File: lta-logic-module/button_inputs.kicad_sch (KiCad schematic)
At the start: 26 parts, among them J5 Conn_01x12, U11 SN74LVC14AD, U12 SN74LVC14AD

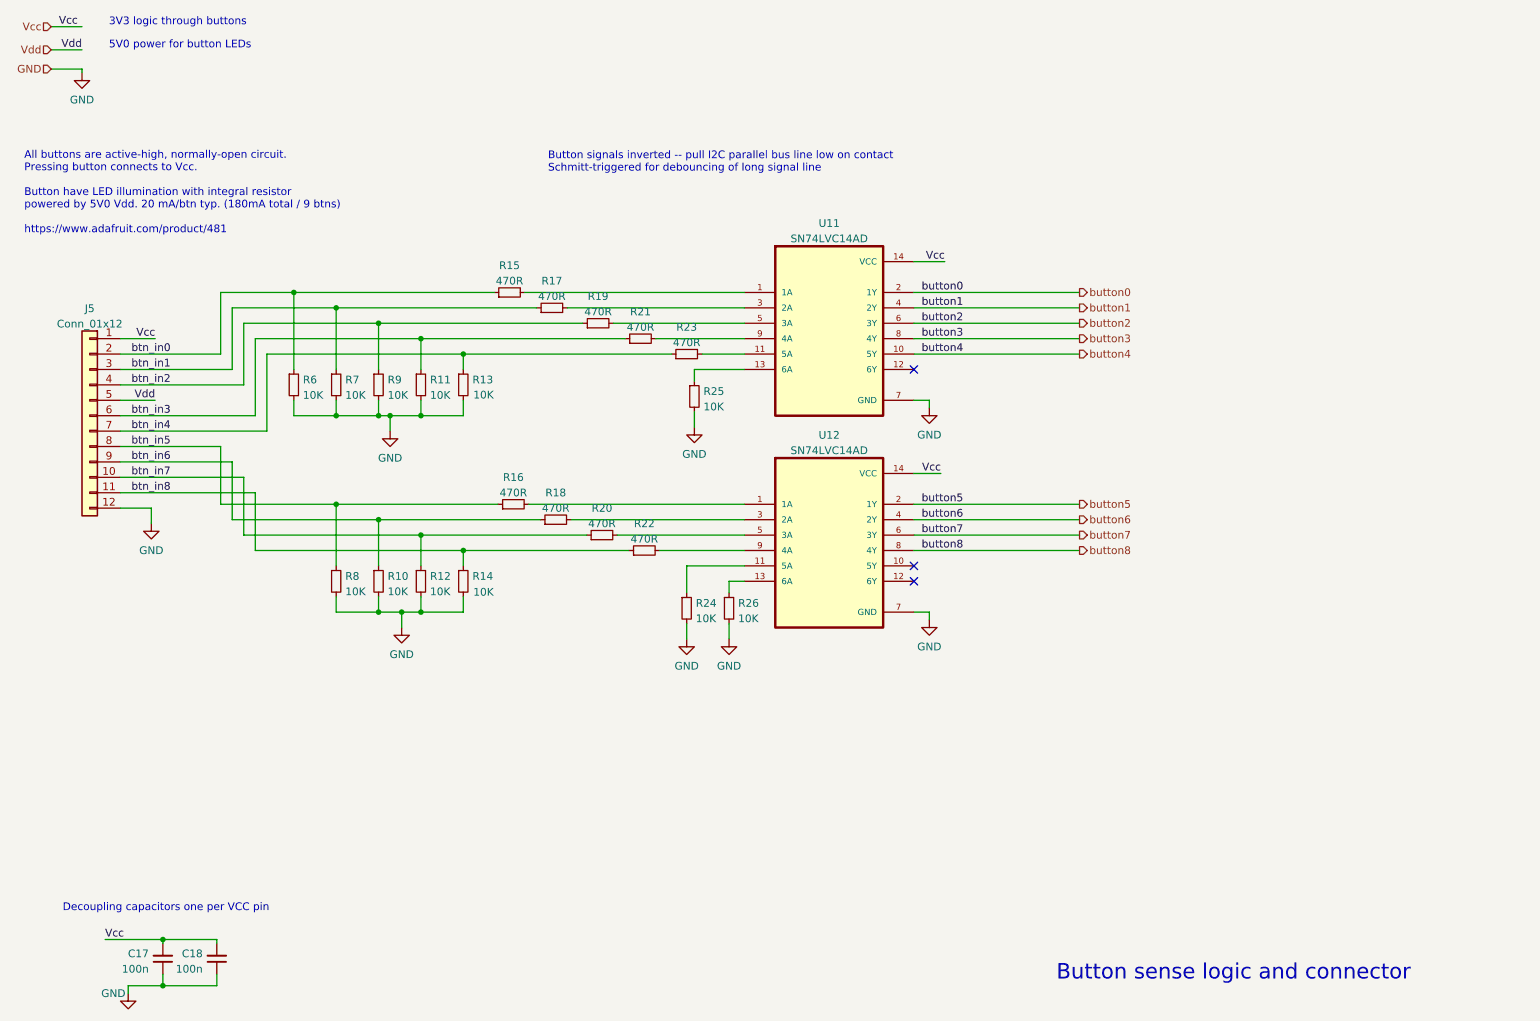
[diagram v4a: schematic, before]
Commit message: Add light sensor circuit.
Adjust TODOs and comments after testing btn circuit.
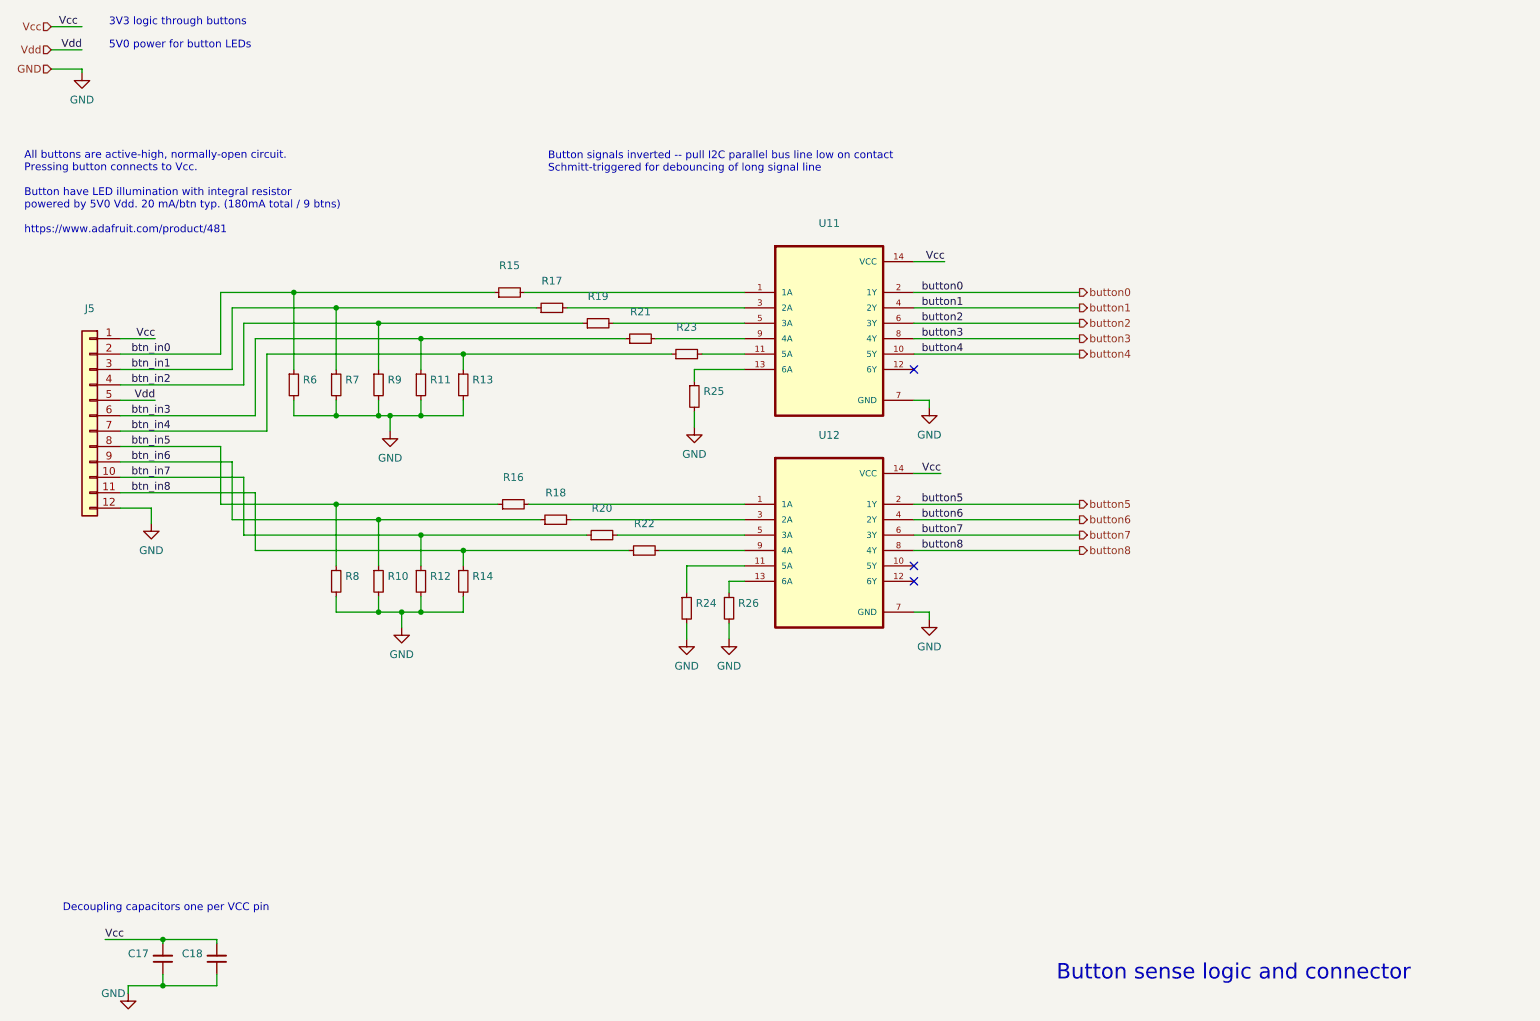
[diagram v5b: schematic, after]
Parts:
- C17, C18: value 100n -> (none); footprint Capacitor_SMD:C_0603_1608Metric -> (none)
- J5: value Conn_01x12 -> (none); footprint Connector_PinHeader_2.54mm:PinHeader_1x12_P2.54mm_Vertical -> (none)
- R10, R11, R12, R13, R14, R24, R25, R26, R6, R7, R8, R9: value 10K -> (none); footprint Resistor_SMD:R_0603_1608Metric -> (none)
- R15, R16, R17, R18, R19, R20, R21, R22, R23: value 470R -> (none); footprint Resistor_SMD:R_0603_1608Metric -> (none)
- U11, U12: value SN74LVC14AD -> (none); footprint Aaron_TI_Parts:TI_SOIC_D_R-PDSO-G14 -> (none)

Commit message: Add main draft of PCB layout for logic module.
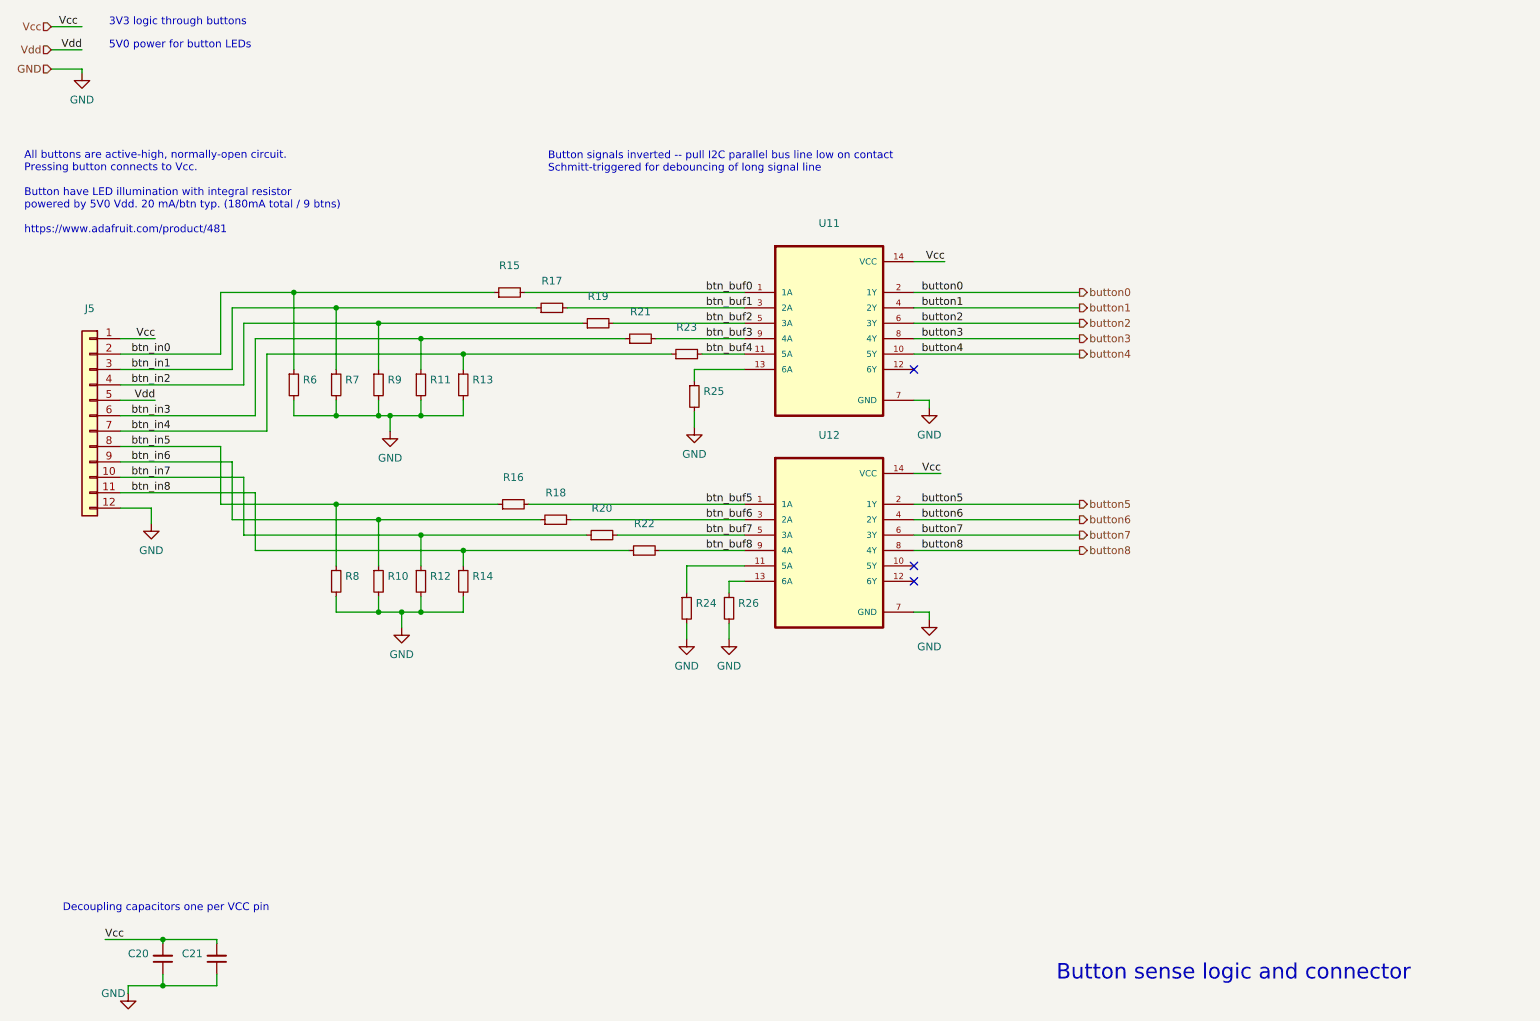
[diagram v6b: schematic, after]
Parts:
- U11, U12: Comment (none) -> Exact MFR/MPN required
- renumbered C17 to C20, C18 to C21
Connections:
- net btn_buf6: now reaches R18.2, U12.3 (2A)
- net btn_buf8: now reaches R22.2, U12.9 (4A)
- net btn_buf2: now reaches R19.2, U11.5 (3A)
- net btn_buf7: now reaches R20.2, U12.5 (3A)
- net btn_buf5: now reaches R16.2, U12.1 (1A)
- net btn_buf3: now reaches R21.2, U11.9 (4A)
- net btn_buf0: now reaches R15.2, U11.1 (1A)
- net btn_buf4: now reaches R23.2, U11.11 (5A)
- net btn_buf1: now reaches R17.2, U11.3 (2A)
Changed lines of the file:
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@@
     (effects (font (size 1.27 1.27)) (justify right bottom))
+  )
+  (label "btn_buf2" (at 128.27 66.675 0)
+    (effects (font (size 1.27 1.27)) (justify left bottom))
   )
   (label "Vcc" (at 37.465 69.215 180)
@@
     (effects (font (size 1.27 1.27)) (justify left bottom))
   )
+  (label "btn_buf4" (at 128.27 71.755 0)
+    (effects (font (size 1.27 1.27)) (justify left bottom))
+  )
   (label "Vdd" (at 37.465 79.375 180)
     (effects (font (size 1.27 1.27)) (justify right bottom))
   )
+  (label "btn_buf1" (at 128.27 64.135 0)
+    (effects (font (size 1.27 1.27)) (justify left bottom))
+  )
   (label "btn_in2" (at 40.005 76.835 180)
     (effects (font (size 1.27 1.27)) (justify right bottom))
@@
     (effects (font (size 1.27 1.27)) (justify right bottom))
   )
+  (label "btn_buf8" (at 128.27 104.14 0)
+    (effects (font (size 1.27 1.27)) (justify left bottom))
+  )
   (label "Vcc" (at 21.59 17.78 0)
     (effects (font (size 1.27 1.27)) (justify left bottom))
   )
+  (label "btn_buf0" (at 128.27 61.595 0)
+    (effects (font (size 1.27 1.27)) (justify left bottom))
+  )
   (label "btn_in3" (at 40.005 81.915 180)
     (effects (font (size 1.27 1.27)) (justify right bottom))
   )
+  (label "btn_buf5" (at 128.27 96.52 0)
+    (effects (font (size 1.27 1.27)) (justify left bottom))
+  )
   (label "button0" (at 163.83 61.595 0)
     (effects (font (size 1.27 1.27)) (justify left bottom))
@@
     (effects (font (size 1.27 1.27)) (justify right bottom))
   )
+  (label "btn_buf6" (at 128.27 99.06 0)
+    (effects (font (size 1.27 1.27)) (justify left bottom))
+  )
+  (label "btn_buf3" (at 128.27 69.215 0)
+    (effects (font (size 1.27 1.27)) (justify left bottom))
+  )
   (label "btn_in6" (at 40.005 89.535 180)
     (effects (font (size 1.27 1.27)) (justify right bottom))
@@
   (label "btn_in8" (at 40.005 94.615 180)
     (effects (font (size 1.27 1.27)) (justify right bottom))
+  )
+  (label "btn_buf7" (at 128.27 101.6 0)
+    (effects (font (size 1.27 1.27)) (justify left bottom))
   )
   (label "button8" (at 163.83 104.14 0)
@@
   (symbol (lib_id "power:GND") (at 36.83 99.695 0) (unit 1)
     (in_bom yes) (on_board yes) (fields_autoplaced)
-    (property "Reference" "#PWR046" (id 0) (at 36.83 106.045 0)
+    (property "Reference" "#PWR047" (id 0) (at 36.83 106.045 0)
       (effects (font (size 1.27 1.27)) hide)
     )
@@
   (symbol (lib_id "Device:C_Small") (at 47.625 171.45 0) (mirror x) (unit 1)
     (in_bom yes) (on_board yes) (fields_autoplaced)
-    (property "Reference" "C18" (id 0) (at 45.3009 170.6089 0)
+    (property "Reference" "C21" (id 0) (at 45.3009 170.6089 0)
       (effects (font (size 1.27 1.27)) (justify right))
     )
@@
   (symbol (lib_id "power:GND") (at 125.095 118.745 0) (unit 1)
     (in_bom yes) (on_board yes) (fields_autoplaced)
-    (property "Reference" "#PWR049" (id 0) (at 125.095 125.095 0)
+    (property "Reference" "#PWR050" (id 0) (at 125.095 125.095 0)
       (effects (font (size 1.27 1.27)) hide)
     )
@@
     )
     (property "MPN" "SN74LVC14AD" (id 5) (at 152.4 104.14 0)
+      (effects (font (size 1.27 1.27)) hide)
+    )
+    (property "Comment" "Exact MFR/MPN required" (id 6) (at 152.4 104.14 0)
       (effects (font (size 1.27 1.27)) hide)
     )
@@
   (symbol (lib_id "power:GND") (at 76.2 84.455 0) (unit 1)
     (in_bom yes) (on_board yes) (fields_autoplaced)
-    (property "Reference" "#PWR047" (id 0) (at 76.2 90.805 0)
+    (property "Reference" "#PWR048" (id 0) (at 76.2 90.805 0)
       (effects (font (size 1.27 1.27)) hide)
     )
@@
   (symbol (lib_id "power:GND") (at 126.365 83.82 0) (unit 1)
     (in_bom yes) (on_board yes) (fields_autoplaced)
-    (property "Reference" "#PWR050" (id 0) (at 126.365 90.17 0)
+    (property "Reference" "#PWR051" (id 0) (at 126.365 90.17 0)
       (effects (font (size 1.27 1.27)) hide)
     )
@@
   (symbol (lib_id "Device:C_Small") (at 38.735 171.45 0) (mirror x) (unit 1)
     (in_bom yes) (on_board yes) (fields_autoplaced)
-    (property "Reference" "C17" (id 0) (at 36.4109 170.6089 0)
+    (property "Reference" "C20" (id 0) (at 36.4109 170.6089 0)
       (effects (font (size 1.27 1.27)) (justify right))
     )
@@
   (symbol (lib_id "power:GND") (at 132.08 118.745 0) (unit 1)
     (in_bom yes) (on_board yes) (fields_autoplaced)
-    (property "Reference" "#PWR051" (id 0) (at 132.08 125.095 0)
+    (property "Reference" "#PWR052" (id 0) (at 132.08 125.095 0)
       (effects (font (size 1.27 1.27)) hide)
     )
@@
   (symbol (lib_id "power:GND") (at 165.1 115.57 0) (unit 1)
     (in_bom yes) (on_board yes) (fields_autoplaced)
-    (property "Reference" "#PWR053" (id 0) (at 165.1 121.92 0)
+    (property "Reference" "#PWR054" (id 0) (at 165.1 121.92 0)
       (effects (font (size 1.27 1.27)) hide)
     )
@@
   (symbol (lib_id "power:GND") (at 78.105 116.84 0) (unit 1)
     (in_bom yes) (on_board yes) (fields_autoplaced)
-    (property "Reference" "#PWR048" (id 0) (at 78.105 123.19 0)
+    (property "Reference" "#PWR049" (id 0) (at 78.105 123.19 0)
       (effects (font (size 1.27 1.27)) hide)
     )
@@
     )
     (property "MPN" "SN74LVC14AD" (id 5) (at 152.4 69.215 0)
+      (effects (font (size 1.27 1.27)) hide)
+    )
+    (property "Comment" "Exact MFR/MPN required" (id 6) (at 152.4 69.215 0)
       (effects (font (size 1.27 1.27)) hide)
     )
@@
   (symbol (lib_id "power:GND") (at 25.4 25.4 0) (unit 1)
     (in_bom yes) (on_board yes) (fields_autoplaced)
-    (property "Reference" "#PWR044" (id 0) (at 25.4 31.75 0)
+    (property "Reference" "#PWR045" (id 0) (at 25.4 31.75 0)
       (effects (font (size 1.27 1.27)) hide)
     )
@@
   (symbol (lib_id "power:GND") (at 33.02 177.165 0) (unit 1)
     (in_bom yes) (on_board yes)
-    (property "Reference" "#PWR045" (id 0) (at 33.02 183.515 0)
+    (property "Reference" "#PWR046" (id 0) (at 33.02 183.515 0)
       (effects (font (size 1.27 1.27)) hide)
     )
@@
   (symbol (lib_id "power:GND") (at 165.1 80.645 0) (unit 1)
     (in_bom yes) (on_board yes) (fields_autoplaced)
-    (property "Reference" "#PWR052" (id 0) (at 165.1 86.995 0)
-      (effects (font (size 1.27 1.27)) hide)
-    )
+    (property "Reference" "#PWR053" (id 0) (at 165.1 86.995 0)
+      (effects (font (size 1.27 1.27)) hide)
+    )

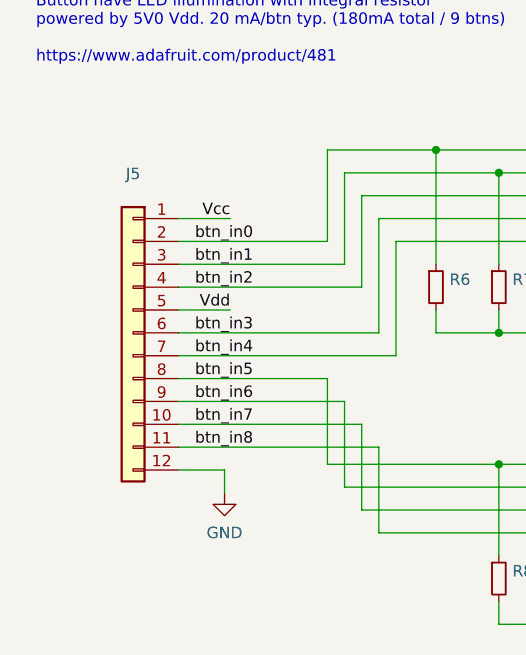
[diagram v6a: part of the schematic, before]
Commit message: Switch 12-pin headers to Molex Micro-Latch c'tors.
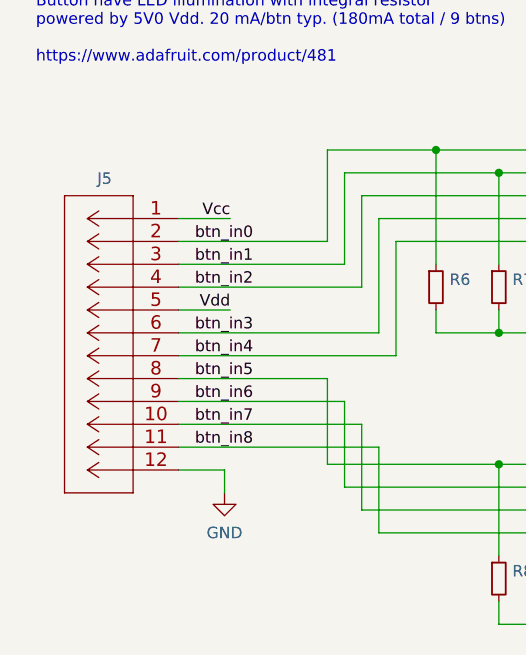
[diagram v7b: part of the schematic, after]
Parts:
- J5: symbol Connector_Generic:Conn_01x12 -> Aaron-Connectors:Molex-MicroLatch-53253-1270; Comment TODO REPLACE FOOTPRINT -> (none); MANUFACTURER (none) -> Molex; MPN XXX TODO FIND -> 532531270
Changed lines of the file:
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@@
     (pin "1")
   )
-  (symbol (lib_id "Connector_Generic:Conn_01x12") (at 26.67 81.915 0) (mirror y) (unit 1)
-    (in_bom yes) (on_board yes) (fields_autoplaced)
-    (property "Reference" "J5" (id 0) (at 26.67 64.2452 0))
-    (property "Value" "" (id 1) (at 26.67 66.7821 0))
-    (property "Footprint" "" (id 2) (at 26.67 81.915 0)
+  (symbol (lib_id "Aaron-Connectors:Molex-MicroLatch-53253-1270") (at 31.75 69.215 0) (mirror y) (unit 1)
+    (in_bom yes) (on_board yes)
+    (property "Reference" "J5" (id 0) (at 23.495 64.77 0))
+    (property "Value" "" (id 1) (at 15.875 83.82 90)
+      (effects (font (size 1.524 1.524)))
+    )
+    (property "Footprint" "" (id 2) (at 22.86 103.505 0)
+      (effects (font (size 1.524 1.524)) hide)
+    )
+    (property "Datasheet" "https://www.molex.com/webdocs/datasheets/pdf/en-us/0532531270_PCB_HEADERS.pdf" (id 3) (at 26.67 60.325 0)
+      (effects (font (size 1.524 1.524)) hide)
+    )
+    (property "Comment" "" (id 4) (at 31.75 69.215 0)
       (effects (font (size 1.27 1.27)) hide)
     )
-    (property "Datasheet" "~" (id 3) (at 26.67 81.915 0)
+    (property "MPN" "532531270" (id 5) (at 25.4 57.785 0)
       (effects (font (size 1.27 1.27)) hide)
     )
-    (property "Comment" "TODO REPLACE FOOTPRINT" (id 4) (at 26.67 81.915 0)
+    (property "MANUFACTURER" "Molex" (id 6) (at 25.4 55.245 0)
       (effects (font (size 1.27 1.27)) hide)
     )
-    (property "MPN" "XXX TODO FIND" (id 5) (at 26.67 81.915 0)
-      (effects (font (size 1.27 1.27)) hide)
-    )

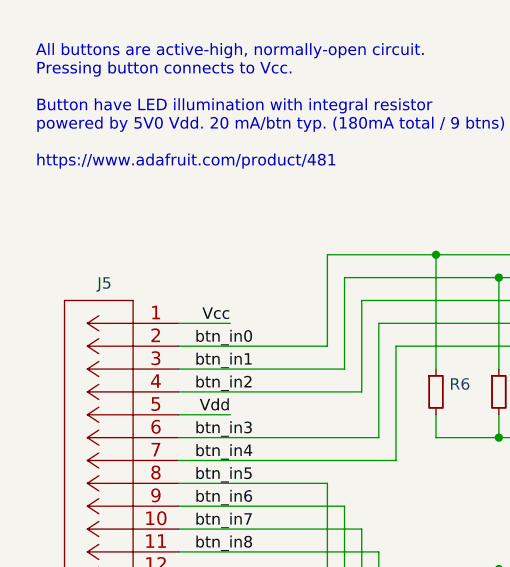
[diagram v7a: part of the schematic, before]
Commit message: Update some footprints to be more accurate.
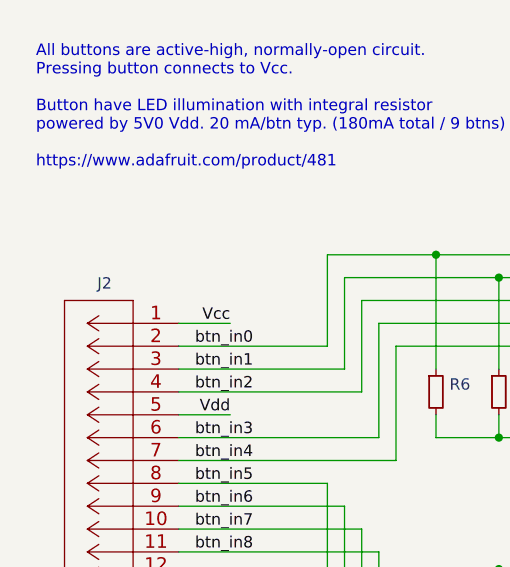
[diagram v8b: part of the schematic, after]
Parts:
- renumbered J5 to J2
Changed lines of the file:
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@@
   (symbol (lib_id "Aaron-Connectors:Molex-MicroLatch-53253-1270") (at 31.75 69.215 0) (mirror y) (unit 1)
     (in_bom yes) (on_board yes)
-    (property "Reference" "J5" (id 0) (at 23.495 64.77 0))
+    (property "Reference" "J2" (id 0) (at 23.495 64.77 0))
     (property "Value" "" (id 1) (at 15.875 83.82 90)
       (effects (font (size 1.524 1.524)))
